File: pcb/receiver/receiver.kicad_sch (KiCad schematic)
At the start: 7 parts, among them J1 Conn_01x05_Socket, J1 WAGO 2061-602, J2 har-flexicon 2,54 MSH-4, J4 Conn_01x02, U1 SP485CN

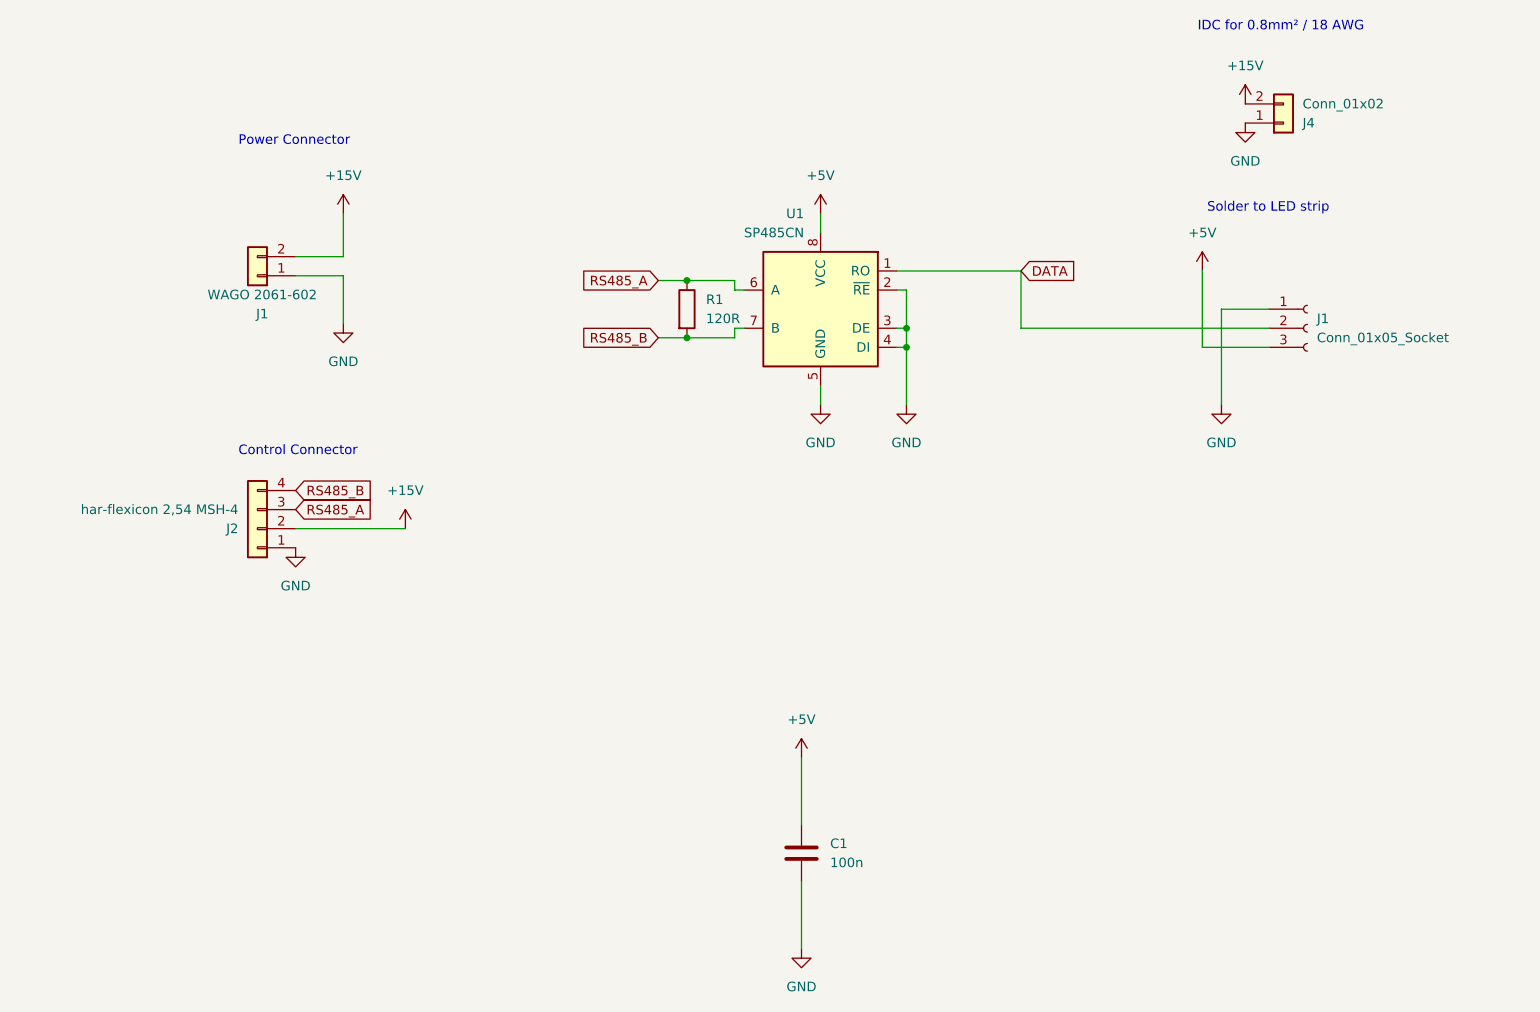
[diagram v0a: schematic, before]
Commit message: Use new FootprintTool
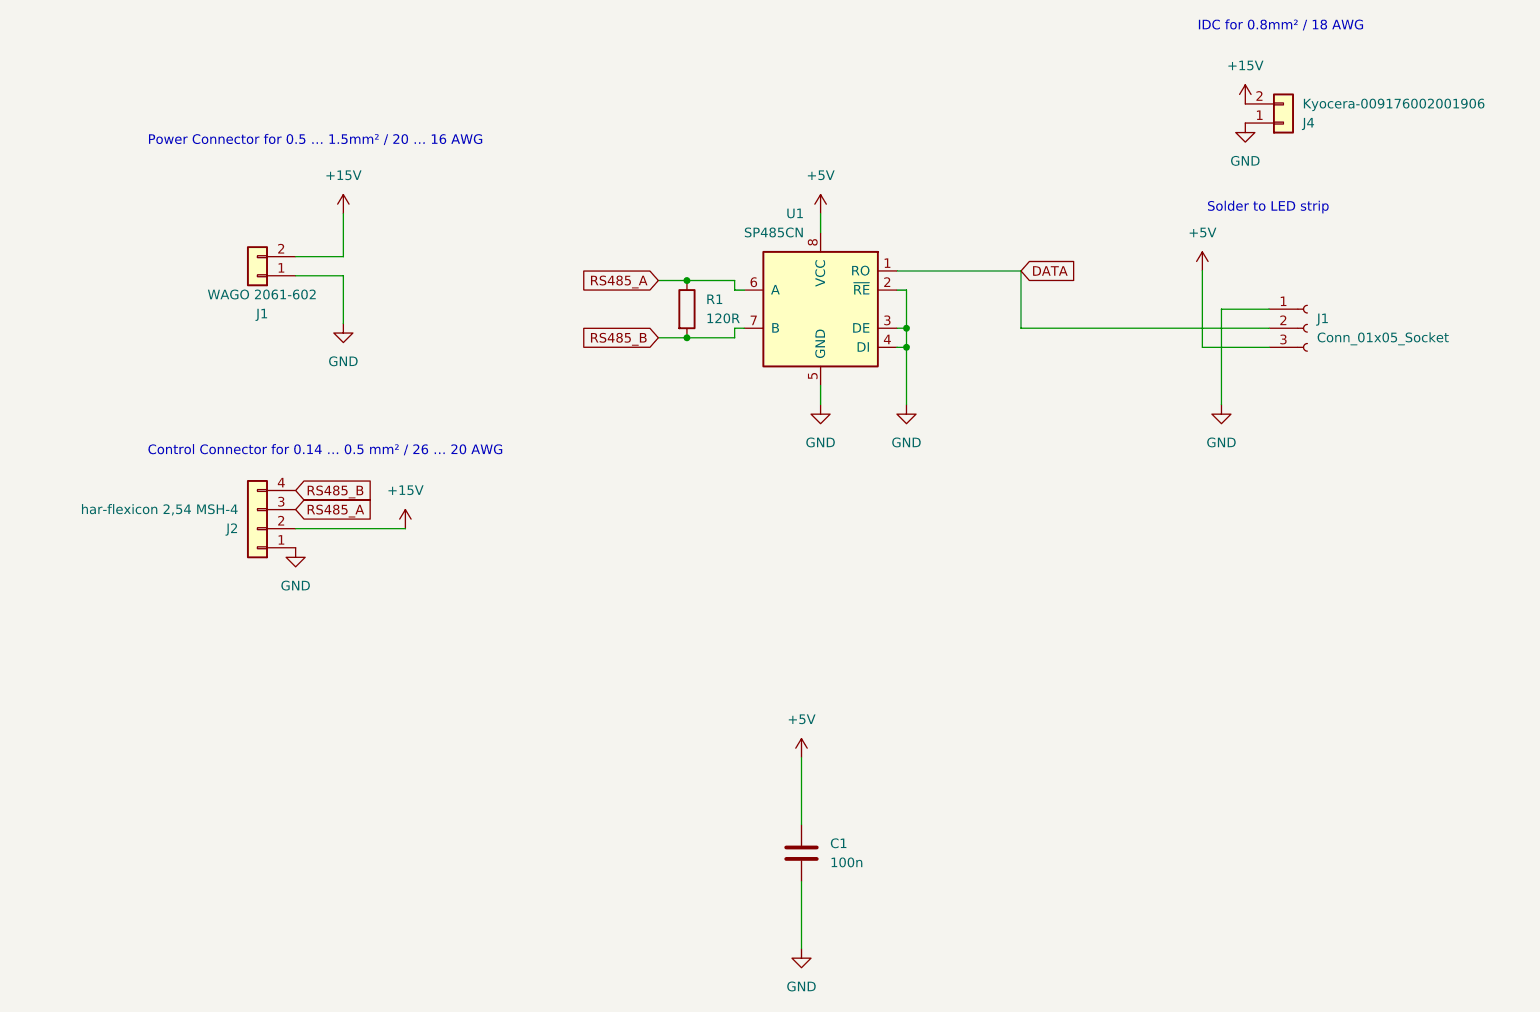
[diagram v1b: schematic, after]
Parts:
- J4: value Conn_01x02 -> Kyocera-009176002001906
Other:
- note added: "Control Connector for 0.14 … 0.5 mm² / 26 … 20 AWG"
- note added: "Power Connector for 0.5 … 1.5mm² / 20 … 16 AWG"
- note removed: "Control Connector"
- note removed: "Power Connector"
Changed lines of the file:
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@@
     (effects (font (size 1.27 1.27)) (justify left bottom))
   )
-  (text "Control Connector" (at 39.37 109.22 0)
+  (text "Control Connector for 0.14 … 0.5 mm² / 26 … 20 AWG"
+    (at 27.305 109.22 0)
     (effects (font (size 1.27 1.27)) (justify left bottom))
   )
@@
     (effects (font (size 1.27 1.27)) (justify left bottom))
   )
-  (text "Power Connector" (at 39.37 67.945 0)
+  (text "Power Connector for 0.5 … 1.5mm² / 20 … 16 AWG" (at 27.305 67.945 0)
     (effects (font (size 1.27 1.27)) (justify left bottom))
   )
@@
       (effects (font (size 1.27 1.27)) (justify left))
     )
-    (property "Value" "Conn_01x02" (at 180.975 62.23 0)
-      (effects (font (size 1.27 1.27)) (justify left))
-    )
+    (property "Value" "Kyocera-009176002001906" (at 180.975 62.23 0)
+      (effects (font (size 1.27 1.27)) (justify left))
+    )
